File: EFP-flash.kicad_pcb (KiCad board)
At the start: 2 copper layers, 30 x 18.4 mm, 17 parts, among them J101 USB_C_Receptacle_USB2.0, J102 Conn_01x06, Q101 MMDT3904, SW101 SW_SPDT, U101 ESD PROTECTION, U102 TLV75533PDBV, U103 CH340C

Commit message: PCB complete
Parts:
- added D102: GREEN, LED_SMD:LED_0603_1608Metric, F.Cu at (151.1, 37.2)
- added J101: USB_B_Micro, Connector_USB_custom:USB_Micro-B_Amphenol_10118194_Horizontal, F.Cu at (127.3, 39.1)
- added LOGO101: Open_Hardware, Symbol:OSHW-Logo2_7.3x6mm_SilkScreen, B.Cu at (145.8, 42.5)
- added R105: 10kΩ, Resistor_SMD:R_0603_1608Metric, F.Cu at (151.1, 35.7)
- moved F101 6.06 mm to (132.7, 42.4), turned to 180 degrees
- moved C101 3.21 mm to (132.7, 40.3), turned to 180 degrees
- moved R101 3.18 mm to (134.0, 51.4)
- moved R102 3.18 mm to (134.0, 45.1)
- moved U101 3.17 mm to (134.0, 48.3)
- moved J102 2.54 mm to (127.0, 48.9)
- moved D101 2.16 mm to (136.5, 36.3)
- moved C104 1.94 mm to (142.7, 35.8)
- moved C102 1.91 mm to (139.1, 35.6)
- moved C103 1.91 mm to (136.5, 39.4)
- moved Q101 1.91 mm to (146.7, 40.6)
- moved R103 1.91 mm to (146.7, 43.8)
- moved SW101 1.91 mm to (151.1, 42.5)
- moved U102 1.91 mm to (133.6, 37.3)
- moved U103 1.91 mm to (141.0, 41.9)
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- renumbered J101 to J102, J102 to J103
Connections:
- J103 pad 2: /SER_TX -> /SER_RX
- J103 pad 3: /SER_RX -> /SER_TX
- U101 pad 1: /USB_D- -> /USB_D+
- U101 pad 6: /USB_D+ -> /USB_D-
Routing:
- net +3V3: track 0.00 -> 37.6 mm, vias 0 -> 4
- net /3v3_{SW}: track 0.00 -> 32.1 mm
- net /USB_D+: track 2.78 -> 33.8 mm
- net /USB_D-: track 2.96 -> 29.4 mm
- net Net-(F101-Pad2): track 0.00 -> 24.6 mm, vias 0 -> 3
- net GND: track 0.00 -> 15.5 mm, vias 0 -> 15
- net VBUS: track 0.00 -> 13.0 mm
- net /SER_RX: track 13.2 -> 19.3 mm
- net Net-(J102-PadA5): track 0.00 -> 4.29 mm
- net /Boot: track 14.9 -> 17.6 mm
- net Net-(J102-PadB5): track 0.00 -> 2.52 mm
- net Net-(D102-Pad1): track 0.00 -> 2.24 mm
- net /EN: track 10.7 -> 12.6 mm
- net /SER_TX: track 16.7 -> 15.9 mm
- added copper zone on B.Cu, net GND
- added copper zone on F.Cu, net GND
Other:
- board size 30 x 18.4 mm -> 28.7 x 20.3 mm
- board text added: "3v3"
- board text added: "Boot"
- board text added: "CP2102 USB->UART"
- board text added: "EN"
- board text added: "ESP-flash v1.0.0"
- board text added: "GND"
- board text added: "JLCJLCJLCJLC"
- board text added: "Rx"
- board text added: "Tx"

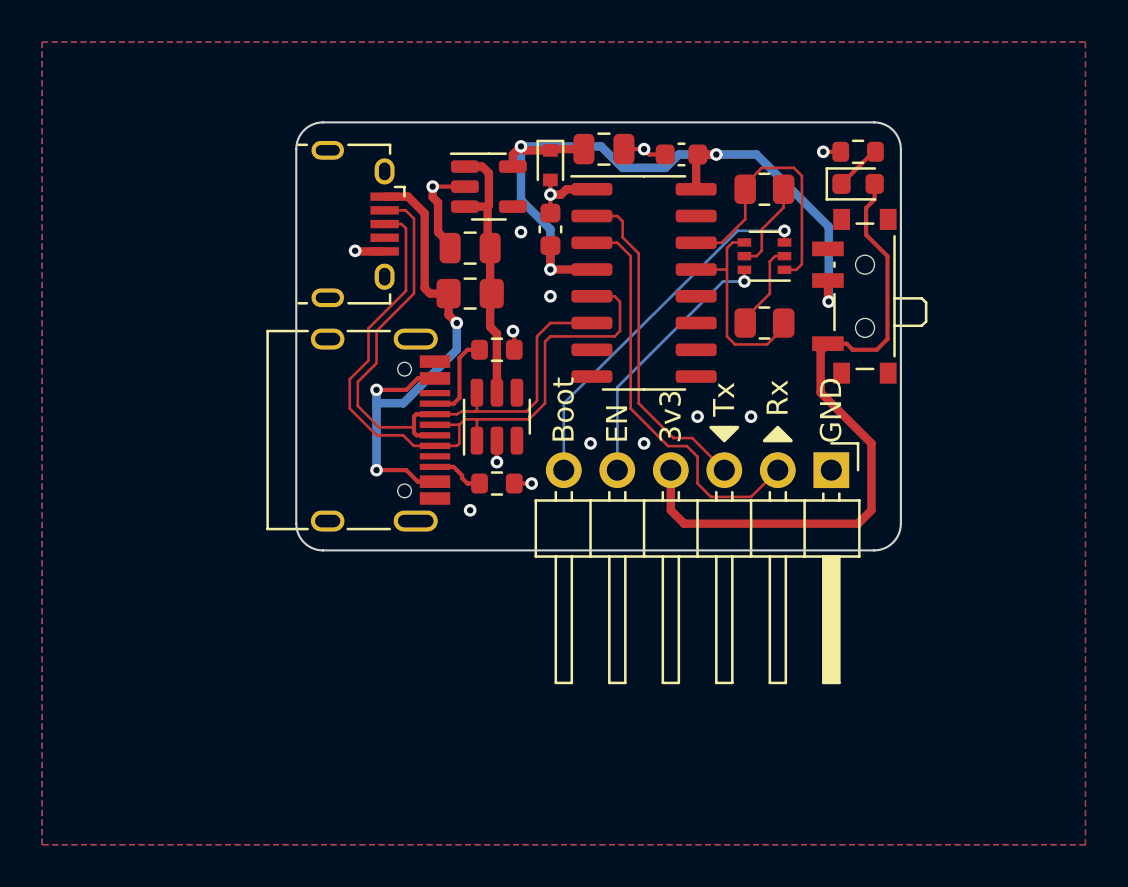
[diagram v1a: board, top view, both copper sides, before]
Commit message: Sent to board fab v1.0.1, replaces previous
Changes:
 - USB diodes out of stock; different manufacturer had their stock.
 - SPDT switch out of stock, replaced with a different switch that
   thankfully also had a footprint in KiCAD
 - Made the board slightly wider to accomodate the switch.
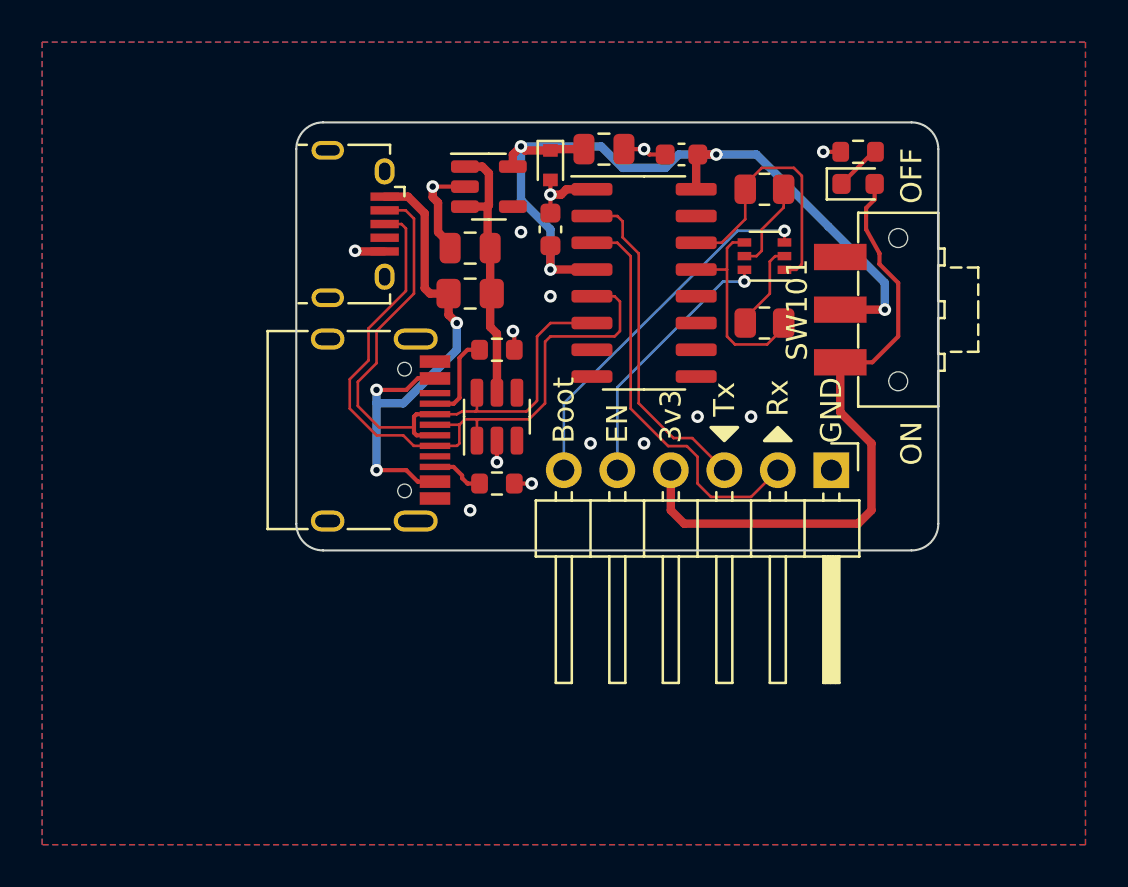
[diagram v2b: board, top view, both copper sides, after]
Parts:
- SW101: footprint Button_Switch_SMD:SW_SPDT_PCM12 -> Button_Switch_SMD:SW_SPDT_CK-JS102011SAQN
- moved SW101 2.01 mm to (153.0, 43.2)
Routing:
- net +3V3: track 37.6 -> 40.2 mm
- net /3v3_{SW}: track 32.1 -> 30.8 mm
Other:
- board size 28.7 x 20.3 mm -> 30.5 x 20.3 mm
- board text added: "ESP-flash v1.1.0"
- board text added: "OFF"
- board text added: "ON"
- board text removed: "ESP-flash v1.0.0"

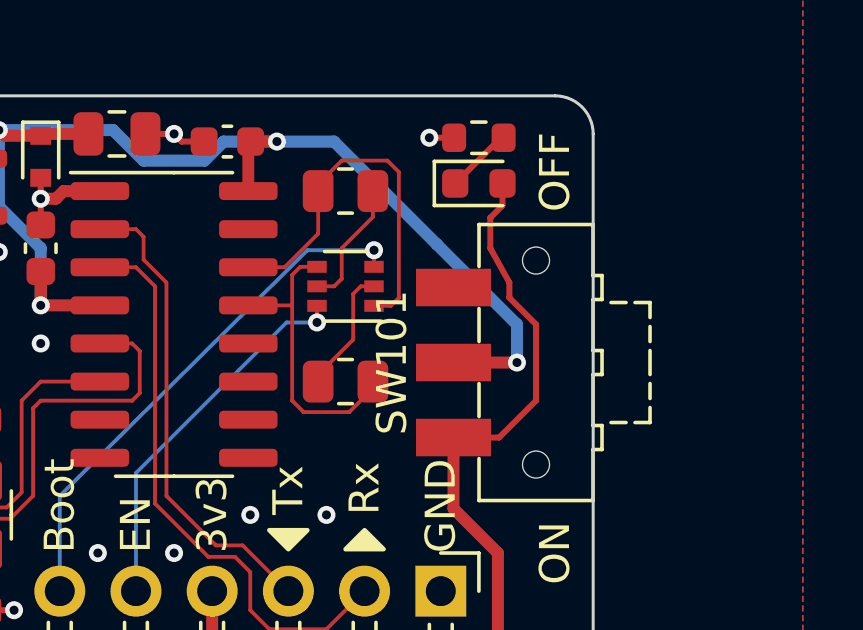
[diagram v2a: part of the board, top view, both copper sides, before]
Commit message: Bugfix: PWR LED backfed from board
Power LED would light up when board was using its own 3v3 Power, even
though the switch was in the off position.

Found a clever solution to fix this, by changing two short traces.
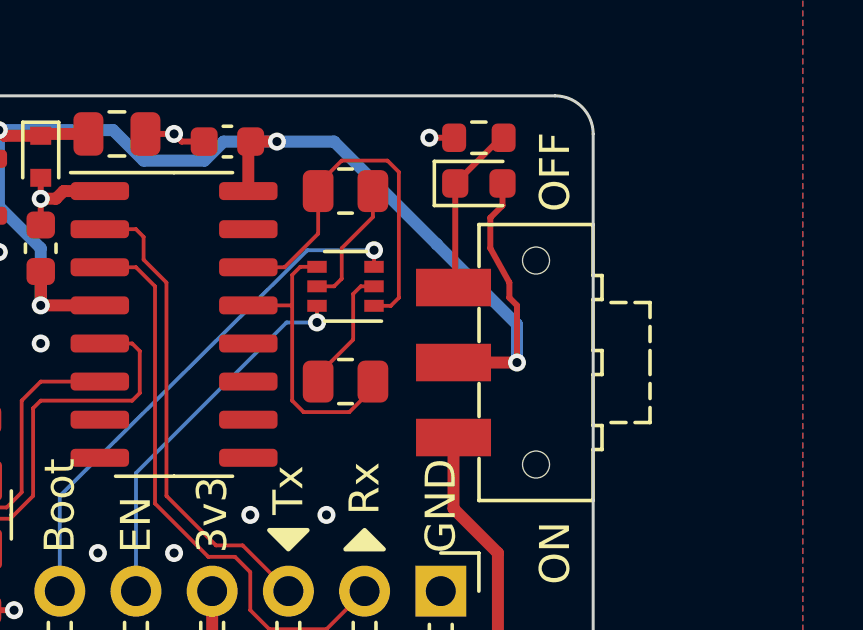
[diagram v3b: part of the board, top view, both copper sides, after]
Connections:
- D102 pad 2: /3v3_{SW} -> +3V3
- SW101 pad 3: unconnected-(SW101-Pad3) -> Net-(D102-Pad1)
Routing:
- net /3v3_{SW}: track 30.8 -> 19.6 mm
- net +3V3: track 40.2 -> 46.6 mm
- net Net-(D102-Pad1): track 2.24 -> 5.74 mm
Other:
- board text added: "${TITLE} ${REVISION}"
- board text removed: "ESP-flash v1.1.0"
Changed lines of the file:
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@@
     (title "ESP-flash")
     (date "2023-01-03")
-    (rev "v1.1.0")
+    (rev "v1.2.0")
     (company "OSH")
     (comment 1 "Drawn by: VGD")
@@
   (net 28 "unconnected-(U101-Pad3)")
   (net 29 "unconnected-(U101-Pad4)")
-  (net 30 "unconnected-(SW101-Pad3)")
-  (net 31 "Net-(D102-Pad1)")
-  (net 32 "unconnected-(J102-PadB8)")
+  (net 30 "Net-(D102-Pad1)")
+  (net 31 "unconnected-(J102-PadB8)")
   (footprint "Resistor_SMD:R_0805_2012Metric" (layer "F.Cu")
     (at 146.685 37.465 180)
@@
     (tags "SOT TO_SOT_SMD")
     (property "JLCPCB_CORRECTION" "0;0;180")
-    (property "LCSC" "C404027")
+    (property "LCSC" "C2937042")
     (property "Sheetfile" "EFP-flash.kicad_sch")
     (property "Sheetname" "")
@@
     (fp_line (start -0.8 0.4125) (end -0.8 -0.4125) (layer "F.Fab") (width 0.1))
     (pad "1" smd roundrect locked (at -0.825 0 180) (size 0.8 0.95) (layers "F.Cu" "F.Paste" "F.Mask") (roundrect_rratio 0.25)
-      (net 31 "Net-(D102-Pad1)") (pintype "passive"))
+      (net 30 "Net-(D102-Pad1)") (pintype "passive"))
     (pad "2" smd roundrect locked (at 0.825 0 180) (size 0.8 0.95) (layers "F.Cu" "F.Paste" "F.Mask") (roundrect_rratio 0.25)
       (net 2 "GND") (pintype "passive"))
@@
     (fp_line (start 0.8 0.4) (end 0.8 -0.4) (layer "F.Fab") (width 0.1))
     (pad "1" smd roundrect locked (at -0.7875 0) (size 0.875 0.95) (layers "F.Cu" "F.Paste" "F.Mask") (roundrect_rratio 0.25)
-      (net 31 "Net-(D102-Pad1)") (pinfunction "K") (pintype "passive"))
+      (net 30 "Net-(D102-Pad1)") (pinfunction "K") (pintype "passive"))
     (pad "2" smd roundrect locked (at 0.7875 0) (size 0.875 0.95) (layers "F.Cu" "F.Paste" "F.Mask") (roundrect_rratio 0.25)
-      (net 12 "/3v3_{SW}") (pinfunction "A") (pintype "passive"))
+      (net 3 "+3V3") (pinfunction "A") (pintype "passive"))
     (model "${KICAD6_3DMODEL_DIR}/LED_SMD.3dshapes/LED_0603_1608Metric.wrl"
       (offset (xyz 0 0 0))
@@
     (descr "Sub-miniature slide switch, right-angle, http://www.ckswitches.com/media/1422/js.pdf")
     (tags "switch spdt")
+    (property "JLCPCB_CORRECTION" "0;-2.75;180")
     (property "LCSC" "C125040")
     (property "Sheetfile" "EFP-flash.kicad_sch")
     (property "Sheetname" "")
     (attr smd)
-    (fp_text reference "SW101" (at 0 -4.8 90) (layer "F.SilkS")
+    (fp_text reference "SW101" (at 0 -4.8 90) (layer "F.SilkS") hide
       (effects (font (size 1 1) (thickness 0.15)))
     )
@@
       (net 3 "+3V3") (pinfunction "B") (pintype "passive"))
     (pad "3" smd rect (at 2.5 -2.75 90) (size 1.25 2.5) (layers "F.Cu" "F.Paste" "F.Mask")
-      (net 30 "unconnected-(SW101-Pad3)") (pinfunction "C") (pintype "passive+no_connect"))
+      (net 30 "Net-(D102-Pad1)") (pinfunction "C") (pintype "passive"))
     (model "${KICAD6_3DMODEL_DIR}/Button_Switch_SMD.3dshapes/SW_SPDT_CK-JS102011SAQN.wrl"
       (offset (xyz 0 0 0))
@@
       (net 7 "/USB_D-") (pinfunction "D-") (pintype "bidirectional"))
     (pad "B8" smd rect locked (at -1.75 -4.045 270) (size 0.3 1.45) (layers "F.Cu" "F.Paste" "F.Mask")
-      (net 32 "unconnected-(J102-PadB8)") (pinfunction "SBU2") (pintype "bidirectional+no_connect"))
+      (net 31 "unconnected-(J102-PadB8)") (pinfunction "SBU2") (pintype "bidirectional+no_connect"))
     (pad "B9" smd rect locked (at -2.45 -4.045 270) (size 0.6 1.45) (layers "F.Cu" "F.Paste" "F.Mask")
       (net 26 "Net-(F101-Pad2)") (pinfunction "VBUS") (pintype "passive"))
@@
     (effects (font (size 1 1) (thickness 0.15)) (justify left mirror))
   )
-  (gr_text "ESP-flash v1.1.0" (at 143.51 36.83) (layer "B.SilkS")
+  (gr_text "${TITLE} ${REVISION}" (at 143.51 36.83) (layer "B.SilkS")
     (effects (font (size 1 1) (thickness 0.15)) (justify mirror))
   )
@@
   (segment (start 138.495 41.275) (end 136.525 41.275) (width 0.4) (layer "F.Cu") (net 3))
   (segment (start 136.525 41.275) (end 136.525 40.145) (width 0.4) (layer "F.Cu") (net 3))
+  (segment (start 152.4 41.275) (end 152.4 43.18) (width 0.2) (layer "F.Cu") (net 3))
   (segment (start 138.115 35.56) (end 136.587 35.56) (width 0.4) (layer "F.Cu") (net 3))
   (segment (start 143.445 35.892) (end 143.523 35.814) (width 0.4) (layer "F.Cu") (net 3))
+  (segment (start 151.511 38.354) (end 151.511 39.37) (width 0.2) (layer "F.Cu") (net 3))
   (segment (start 136.525 35.622) (end 135.317 35.622) (width 0.4) (layer "F.Cu") (net 3))
+  (segment (start 151.9175 37.9475) (end 151.511 38.354) (width 0.2) (layer "F.Cu") (net 3))
   (segment (start 143.523 35.814) (end 144.399 35.814) (width 0.4) (layer "F.Cu") (net 3))
+  (segment (start 152.146 41.021) (end 152.4 41.275) (width 0.2) (layer "F.Cu") (net 3))
   (segment (start 152.4 43.18) (end 150.285 43.18) (width 0.4) (layer "F.Cu") (net 3))
+  (segment (start 152.146 40.513) (end 152.146 41.021) (width 0.2) (layer "F.Cu") (net 3))
   (segment (start 135.317 35.622) (end 135.128 35.433) (width 0.4) (layer "F.Cu") (net 3))
   (segment (start 136.587 35.56) (end 136.525 35.622) (width 0.4) (layer "F.Cu") (net 3))
+  (segment (start 151.511 39.37) (end 152.146 40.513) (width 0.2) (layer "F.Cu") (net 3))
   (segment (start 143.445 37.465) (end 143.445 35.892) (width 0.4) (layer "F.Cu") (net 3))
+  (segment (start 151.9175 37.211) (end 151.9175 37.9475) (width 0.2) (layer "F.Cu") (net 3))
   (segment (start 134.7415 35.8195) (end 135.128 35.433) (width 0.4) (layer "F.Cu") (net 3))
   (via (at 135.128 35.433) (size 0.6) (drill 0.3) (layers "F.Cu" "B.Cu") (net 3))
@@
   (segment (start 143.002 49.657) (end 143.51 50.165) (width 0.127) (layer "F.Cu") (net 11))
   (segment (start 143.51 50.165) (end 143.51 51.435) (width 0.127) (layer "F.Cu") (net 11))
-  (segment (start 151.805 45.68) (end 150.285 45.68) (width 0.2) (layer "F.Cu") (net 12))
   (segment (start 151.765 49.53) (end 150.285 48.05) (width 0.4) (layer "F.Cu") (net 12))
-  (segment (start 151.511 38.354) (end 151.511 39.37) (width 0.2) (layer "F.Cu") (net 12))
   (segment (start 142.875 53.34) (end 142.24 52.705) (width 0.4) (layer "F.Cu") (net 12))
   (segment (start 150.285 48.05) (end 150.285 45.68) (width 0.4) (layer "F.Cu") (net 12))
-  (segment (start 151.9175 37.9475) (end 151.511 38.354) (width 0.2) (layer "F.Cu") (net 12))
   (segment (start 151.765 49.53) (end 151.765 52.705) (width 0.4) (layer "F.Cu") (net 12))
   (segment (start 142.24 52.705) (end 142.24 50.8) (width 0.4) (layer "F.Cu") (net 12))
-  (segment (start 153.035 41.91) (end 153.035 44.45) (width 0.2) (layer "F.Cu") (net 12))
   (segment (start 151.13 53.34) (end 142.875 53.34) (width 0.4) (layer "F.Cu") (net 12))
-  (segment (start 153.035 44.45) (end 151.805 45.68) (width 0.2) (layer "F.Cu") (net 12))
   (segment (start 151.765 52.705) (end 151.13 53.34) (width 0.4) (layer "F.Cu") (net 12))
-  (segment (start 152.146 40.513) (end 152.146 41.021) (width 0.2) (layer "F.Cu") (net 12))
-  (segment (start 151.511 39.37) (end 152.146 40.513) (width 0.2) (layer "F.Cu") (net 12))
-  (segment (start 151.9175 37.211) (end 151.9175 37.9475) (width 0.2) (layer "F.Cu") (net 12))
-  (segment (start 152.146 41.021) (end 153.035 41.91) (width 0.2) (layer "F.Cu") (net 12))
   (segment (start 145.735 41.29) (end 145.735 41.844) (width 0.127) (layer "F.Cu") (net 13))
   (via (at 145.735 41.844) (size 0.6) (drill 0.3) (layers "F.Cu" "B.Cu") (net 13))
@@
   (segment (start 132.08 45.085) (end 132.08 43.815) (width 0.4) (layer "B.Cu") (net 26))
   (segment (start 128.27 47.625) (end 128.27 46.99) (width 0.4) (layer "B.Cu") (net 26))
-  (segment (start 150.3425 37.211) (end 151.8665 35.687) (width 0.2) (layer "F.Cu") (net 31))
-  (segment (start 151.8665 35.687) (end 151.955 35.687) (width 0.2) (layer "F.Cu") (net 31))
+  (segment (start 150.3425 37.211) (end 150.3425 40.6225) (width 0.2) (layer "F.Cu") (net 30))
+  (segment (start 150.3425 37.211) (end 151.8665 35.687) (width 0.2) (layer "F.Cu") (net 30))
+  (segment (start 151.8665 35.687) (end 151.955 35.687) (width 0.2) (layer "F.Cu") (net 30))
+  (segment (start 150.3425 40.6225) (end 150.285 40.68) (width 0.2) (layer "F.Cu") (net 30))
   (zone (net 2) (net_name "GND") (layers F&B.Cu) (hatch edge 0.508)
     (connect_pads (clearance 0.254))
